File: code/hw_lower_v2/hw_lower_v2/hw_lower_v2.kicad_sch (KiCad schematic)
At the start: 26 parts, among them J1 Screw_Terminal_01x01, J2 Screw_Terminal_01x01, J3 Screw_Terminal_01x01, J4 Screw_Terminal_01x01, J5 Screw_Terminal_01x01, J6 Screw_Terminal_01x01, J7 Conn_01x06_Pin, J8 Conn_02x20_Odd_Even

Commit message: have one project part library
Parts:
- J1, J2, J3, J4, J5, J6: footprint JLCPCB:CONN-TH_T44001 -> multi_new:CONN-TH_T44001
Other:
- moved on the sheet: J1, J2, J3

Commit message: routed most of the board
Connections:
- net AC/GFCI_CALIBRATE: now also J8.9 (Pin_9); no longer J8.21 (Pin_21)
- net AC/GFCI_FAULT: now also J8.11 (Pin_11); no longer J8.19 (Pin_19)
- net AC/GFCI_TEST: now also J8.7 (Pin_7); no longer J8.23 (Pin_23)
- net AC/POWER_MEASUREMENT_INFO: now also J8.19 (Pin_19); no longer J8.11 (Pin_11)

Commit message: layout 99% finished
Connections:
- net +12V: now also J8.21 (Pin_21), J8.23 (Pin_23); no longer J8.1 (Pin_1)
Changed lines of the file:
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@@
 	)
 	(junction
+		(at 240.03 93.98)
+		(diameter 0)
+		(color 0 0 0 0)
+	)
+	(junction
 		(at 257.81 81.28)
 		(diameter 0)
@@
 	(wire
 		(pts
+			(xy 240.03 93.98) (xy 240.03 96.52)
+		)
+		(stroke
+			(width 0)
+			(type default)
+		)
+	)
+	(wire
+		(pts
 			(xy 69.85 49.53) (xy 69.85 68.58)
 		)
@@
 	(wire
 		(pts
+			(xy 240.03 93.98) (xy 242.57 93.98)
+		)
+		(stroke
+			(width 0)
+			(type default)
+		)
+	)
+	(wire
+		(pts
 			(xy 240.03 71.12) (xy 242.57 71.12)
 		)
@@
 	(wire
 		(pts
-			(xy 240.03 68.58) (xy 242.57 68.58)
+			(xy 257.81 96.52) (xy 257.81 99.06)
 		)
 		(stroke
@@
 	(wire
 		(pts
-			(xy 257.81 96.52) (xy 257.81 99.06)
+			(xy 255.27 78.74) (xy 257.81 78.74)
 		)
 		(stroke
@@
 	(wire
 		(pts
-			(xy 255.27 78.74) (xy 257.81 78.74)
+			(xy 242.57 96.52) (xy 240.03 96.52)
 		)
 		(stroke
@@
 	)
 	(symbol
-		(lib_id "power:+12V")
-		(at 240.03 68.58 90)
-		(unit 1)
-		(exclude_from_sim no)
-		(in_bom yes)
-		(on_board yes)
-		(dnp no)
-		(fields_autoplaced yes)
-		(property "Reference" "#PWR03"
-			(at 243.84 68.58 0)
-			(effects
-				(font
-					(size 1.27 1.27)
-				)
-				(hide yes)
-			)
-		)
-		(property "Value" "+12V"
-			(at 236.22 68.5799 90)
-			(effects
-				(font
-					(size 1.27 1.27)
-				)
-				(justify left)
-			)
-		)
-		(property "Footprint" ""
-			(at 240.03 68.58 0)
-			(effects
-				(font
-					(size 1.27 1.27)
-				)
-				(hide yes)
-			)
-		)
-		(property "Datasheet" ""
-			(at 240.03 68.58 0)
-			(effects
-				(font
-					(size 1.27 1.27)
-				)
-				(hide yes)
-			)
-		)
-		(property "Description" "Power symbol creates a global label with name \"+12V\""
-			(at 240.03 68.58 0)
-			(effects
-				(font
-					(size 1.27 1.27)
-				)
-				(hide yes)
-			)
-		)
-		(pin "1"
-		)
-		(instances
-			(project "hw_lower_v2"
-				(path "/c5175f1c-553a-46da-abbd-483c59ad8dfa"
-					(reference "#PWR03")
-					(unit 1)
-				)
-			)
-		)
-	)
-	(symbol
 		(lib_id "Connector:Conn_01x06_Pin")
 		(at 36.83 109.22 0)
@@
 					(unit 1)
 				)
+			)
+		)
+	)
+	(symbol
+		(lib_id "power:+12V")
+		(at 240.03 93.98 90)
+		(unit 1)
+		(exclude_from_sim no)
+		(in_bom yes)
+		(on_board yes)
+		(dnp no)
+		(fields_autoplaced yes)
+		(property "Reference" "#PWR03"
+			(at 243.84 93.98 0)
+			(effects
+				(font
+					(size 1.27 1.27)
+				)
+				(hide yes)
+			)
+		)
+		(property "Value" "+12V"
+			(at 236.22 93.9799 90)
+			(effects
+				(font
+					(size 1.27 1.27)
+				)
+				(justify left)
+			)
+		)
+		(property "Footprint" ""
+			(at 240.03 93.98 0)
+			(effects
+				(font
+					(size 1.27 1.27)
+				)
+				(hide yes)
+			)
+		)
+		(property "Datasheet" ""
+			(at 240.03 93.98 0)
+			(effects
+				(font
+					(size 1.27 1.27)
+				)
+				(hide yes)
+			)
+		)
+		(property "Description" "Power symbol creates a global label with name \"+12V\""
+			(at 240.03 93.98 0)
+			(effects
+				(font
+					(size 1.27 1.27)
+				)
+				(hide yes)
+			)
+		)
+		(pin "1"
+		)
+		(instances
+			(project "hw_lower_v2"
+				(path "/c5175f1c-553a-46da-abbd-483c59ad8dfa"
+					(reference "#PWR03")
+					(unit 1)
+				)

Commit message: simplify component values
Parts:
- R2, R4, R6: value 100K -> 10K; LCSC C25803 -> C25804
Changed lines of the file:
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@@
 			)
 		)
-		(property "Value" "100K"
+		(property "Value" "10K"
 			(at 232.918 148.082 0)
 			(effects
@@
 			)
 		)
-		(property "LCSC" "C25803"
+		(property "LCSC" "C25804"
 			(at 237.49 147.32 0)
 			(effects
@@
 			)
 		)
-		(property "Value" "100K"
+		(property "Value" "10K"
 			(at 251.206 148.336 0)
 			(effects
@@
 			)
 		)
-		(property "LCSC" "C25803"
+		(property "LCSC" "C25804"
 			(at 255.27 147.32 0)
 			(effects
@@
 			)
 		)
-		(property "Value" "100K"
+		(property "Value" "10K"
 			(at 242.316 148.336 0)
 			(effects
@@
 			)
 		)
-		(property "LCSC" "C25803"
+		(property "LCSC" "C25804"
 			(at 246.38 147.32 0)
 			(effects

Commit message: made a full reposition of the whole pcb. When I get everything working, the milkv module can be on the bottom pcb and all the device specific devices can be on the other pcb. Also now conceptualy, the current board can be broken onto two, and be made into a thin long one
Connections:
- net EVSE control and status/CONTROL_PILOT_OUT: now also J7.5 (Pin_5); no longer J7.1 (Pin_1)
- net EVSE control and status/LOCK_SENSE_GND: now also J7.2 (Pin_2); no longer J7.6 (Pin_6)
- net EVSE control and status/LOCK_SENSE_OUT: now also J7.1 (Pin_1); no longer J7.5 (Pin_5)
- net EVSE control and status/PROXIMITY_PILOT: now also J7.6 (Pin_6); no longer J7.2 (Pin_2)
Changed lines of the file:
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@@
 	(wire
 		(pts
+			(xy 41.91 104.14) (xy 72.39 104.14)
+		)
+		(stroke
+			(width 0)
+			(type default)
+		)
+	)
+	(wire
+		(pts
 			(xy 209.55 78.74) (xy 209.55 86.36)
 		)
@@
 	(wire
 		(pts
-			(xy 41.91 77.47) (xy 44.45 77.47)
+			(xy 41.91 106.68) (xy 72.39 106.68)
 		)
 		(stroke
@@
 	(wire
 		(pts
-			(xy 72.39 111.76) (xy 66.04 111.76)
+			(xy 41.91 114.3) (xy 72.39 114.3)
 		)
 		(stroke
@@
 	(wire
 		(pts
-			(xy 255.27 76.2) (xy 257.81 76.2)
+			(xy 41.91 77.47) (xy 44.45 77.47)
 		)
 		(stroke
@@
 	(wire
 		(pts
-			(xy 119.38 81.28) (xy 207.01 81.28)
+			(xy 255.27 76.2) (xy 257.81 76.2)
 		)
 		(stroke
@@
 	(wire
 		(pts
-			(xy 119.38 71.12) (xy 214.63 71.12)
+			(xy 119.38 81.28) (xy 207.01 81.28)
 		)
 		(stroke
@@
 	(wire
 		(pts
-			(xy 257.81 101.6) (xy 257.81 104.14)
+			(xy 119.38 71.12) (xy 214.63 71.12)
 		)
 		(stroke
@@
 	(wire
 		(pts
-			(xy 261.62 114.3) (xy 261.62 124.46)
+			(xy 257.81 101.6) (xy 257.81 104.14)
 		)
 		(stroke
@@
 	(wire
 		(pts
-			(xy 66.04 111.76) (xy 66.04 106.68)
+			(xy 261.62 114.3) (xy 261.62 124.46)
 		)
 		(stroke
@@
 	(wire
 		(pts
-			(xy 60.96 111.76) (xy 41.91 111.76)
-		)
-		(stroke
-			(width 0)
-			(type default)
-		)
-	)
-	(wire
-		(pts
 			(xy 186.69 101.6) (xy 242.57 101.6)
 		)
@@
 	(wire
 		(pts
-			(xy 72.39 125.73) (xy 55.88 125.73)
+			(xy 240.03 121.92) (xy 240.03 142.24)
 		)
 		(stroke
@@
 	(wire
 		(pts
-			(xy 240.03 121.92) (xy 240.03 142.24)
+			(xy 41.91 85.09) (xy 44.45 85.09)
 		)
 		(stroke
@@
 	(wire
 		(pts
-			(xy 41.91 85.09) (xy 44.45 85.09)
+			(xy 41.91 116.84) (xy 72.39 116.84)
 		)
 		(stroke
@@
 	(wire
 		(pts
-			(xy 55.88 125.73) (xy 55.88 116.84)
-		)
-		(stroke
-			(width 0)
-			(type default)
-		)
-	)
-	(wire
-		(pts
 			(xy 255.27 73.66) (xy 257.81 73.66)
 		)
@@
 	(wire
 		(pts
-			(xy 60.96 120.65) (xy 60.96 111.76)
+			(xy 41.91 72.39) (xy 72.39 72.39)
 		)
 		(stroke
@@
 	(wire
 		(pts
-			(xy 41.91 72.39) (xy 72.39 72.39)
+			(xy 41.91 111.76) (xy 72.39 111.76)
 		)
 		(stroke
@@
 	(wire
 		(pts
-			(xy 55.88 116.84) (xy 41.91 116.84)
-		)
-		(stroke
-			(width 0)
-			(type default)
-		)
-	)
-	(wire
-		(pts
 			(xy 219.71 76.2) (xy 219.71 66.04)
 		)
@@
 	(wire
 		(pts
-			(xy 66.04 106.68) (xy 41.91 106.68)
+			(xy 191.77 114.3) (xy 242.57 114.3)
 		)
 		(stroke
@@
 	(wire
 		(pts
-			(xy 191.77 114.3) (xy 242.57 114.3)
+			(xy 259.08 121.92) (xy 259.08 116.84)
 		)
 		(stroke
@@
 	(wire
 		(pts
-			(xy 259.08 121.92) (xy 259.08 116.84)
+			(xy 41.91 87.63) (xy 72.39 87.63)
 		)
 		(stroke
@@
 	(wire
 		(pts
-			(xy 41.91 87.63) (xy 72.39 87.63)
+			(xy 41.91 109.22) (xy 72.39 109.22)
 		)
 		(stroke
@@
 	(wire
 		(pts
-			(xy 63.5 109.22) (xy 41.91 109.22)
-		)
-		(stroke
-			(width 0)
-			(type default)
-		)
-	)
-	(wire
-		(pts
 			(xy 119.38 111.76) (xy 186.69 111.76)
 		)
@@
 	(wire
 		(pts
-			(xy 63.5 118.11) (xy 63.5 109.22)
-		)
-		(stroke
-			(width 0)
-			(type default)
-		)
-	)
-	(wire
-		(pts
 			(xy 262.89 71.12) (xy 262.89 68.58)
 		)
@@
 	(wire
 		(pts
-			(xy 72.39 118.11) (xy 63.5 118.11)
-		)
-		(stroke
-			(width 0)
-			(type default)
-		)
-	)
-	(wire
-		(pts
 			(xy 194.31 116.84) (xy 242.57 116.84)
 		)
@@
 	(wire
 		(pts
-			(xy 72.39 120.65) (xy 60.96 120.65)
-		)
-		(stroke
-			(width 0)
-			(type default)
-		)
-	)
-	(wire
-		(pts
 			(xy 214.63 81.28) (xy 242.57 81.28)
 		)
@@
 	(wire
 		(pts
-			(xy 72.39 123.19) (xy 58.42 123.19)
-		)
-		(stroke
-			(width 0)
-			(type default)
-		)
-	)
-	(wire
-		(pts
 			(xy 246.38 142.24) (xy 246.38 143.51)
 		)
@@
 	(wire
 		(pts
-			(xy 58.42 114.3) (xy 41.91 114.3)
-		)
-		(stroke
-			(width 0)
-			(type default)
-		)
-	)
-	(wire
-		(pts
-			(xy 58.42 123.19) (xy 58.42 114.3)
-		)
-		(stroke
-			(width 0)
-			(type default)
-		)
-	)
-	(wire
-		(pts
 			(xy 257.81 78.74) (xy 257.81 81.28)
 		)
@@
 		)
 	)
-	(wire
-		(pts
-			(xy 41.91 104.14) (xy 72.39 104.14)
-		)
-		(stroke
-			(width 0)
-			(type default)
-		)
-	)
 	(text "BOARD VERSION: V0"
 		(exclude_from_sim no)
@@
 		)
 		(pin "PROXIMITY_PILOT" input
-			(at 72.39 111.76 180)
+			(at 72.39 116.84 180)
 			(effects
 				(font
@@
 		)
 		(pin "LOCK_A_OUT" input
-			(at 72.39 118.11 180)
+			(at 72.39 109.22 180)
 			(effects
 				(font
@@
 		)
 		(pin "LOCK_B_OUT" input
-			(at 72.39 120.65 180)
+			(at 72.39 111.76 180)
 			(effects
 				(font
@@
 		)
 		(pin "CONTROL_PILOT_OUT" input
-			(at 72.39 104.14 180)
+			(at 72.39 114.3 180)
 			(effects
 				(font
@@
 		)
 		(pin "LOCK_SENSE_GND" input
-			(at 72.39 125.73 180)
+			(at 72.39 106.68 180)
 			(effects
 				(font
@@
 		)
 		(pin "LOCK_SENSE_OUT" input
-			(at 72.39 123.19 180)
+			(at 72.39 104.14 180)
 			(effects
 				(font

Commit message: Relalaid out the LV part of the board.
One or two small things left to do.
Prepared for the 2.0 version of the PCB where the duo01 module can be
put on the lower board.
Also it is possible to make a sandwitch situation, and make a long thin
product.
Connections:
- net +5V: no longer names the net of J8.3 (Pin_3)
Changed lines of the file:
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@@
-	(wire
-		(pts
-			(xy 240.03 71.12) (xy 242.57 71.12)
-		)
-		(stroke
-			(width 0)
-			(type default)
-		)
-	)
 	(wire
 		(pts
@@
 					(unit 1)
 				)
-			)
-		)
-	)
-	(symbol
-		(lib_id "power:+5V")
-		(at 240.03 71.12 90)
-		(unit 1)
-		(exclude_from_sim no)
-		(in_bom yes)
-		(on_board yes)
-		(dnp no)
-		(property "Reference" "#PWR04"
-			(at 243.84 71.12 0)
-			(effects
-				(font
-					(size 1.27 1.27)
-				)
-				(hide yes)
-			)
-		)
-		(property "Value" "+5V"
-			(at 232.918 71.12 90)
-			(effects
-				(font
-					(size 1.27 1.27)
-				)
-			)
-		)
-		(property "Footprint" ""
-			(at 240.03 71.12 0)
-			(effects
-				(font
-					(size 1.27 1.27)
-				)
-				(hide yes)
-			)
-		)
-		(property "Datasheet" ""
-			(at 240.03 71.12 0)
-			(effects
-				(font
-					(size 1.27 1.27)
-				)
-				(hide yes)
-			)
-		)
-		(property "Description" "Power symbol creates a global label with name \"+5V\""
-			(at 240.03 71.12 0)
-			(effects
-				(font
-					(size 1.27 1.27)
-				)
-				(hide yes)
-			)
-		)
-		(pin "1"
-		)
-		(instances
-			(project "hw_lower_v2"
-				(path "/c5175f1c-553a-46da-abbd-483c59ad8dfa"
-					(reference "#PWR04")
-					(unit 1)
-				)

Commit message: almost ready :-)
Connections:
- net +3.3V: now also J8.1 (Pin_1), J8.3 (Pin_3)
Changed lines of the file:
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@@
+	)
+	(junction
+		(at 240.03 71.12)
+		(diameter 0)
+		(color 0 0 0 0)
 	)
 	(junction
@@
 		(color 0 0 0 0)
 	)
+	(junction
+		(at 240.03 73.66)
+		(diameter 0)
+		(color 0 0 0 0)
+	)
+	(wire
+		(pts
+			(xy 240.03 68.58) (xy 240.03 71.12)
+		)
+		(stroke
+			(width 0)
+			(type default)
+		)
+	)
 	(wire
 		(pts
@@
 	(wire
 		(pts
+			(xy 240.03 71.12) (xy 240.03 73.66)
+		)
+		(stroke
+			(width 0)
+			(type default)
+		)
+	)
+	(wire
+		(pts
 			(xy 257.81 99.06) (xy 257.81 101.6)
 		)
@@
 	(wire
 		(pts
+			(xy 240.03 71.12) (xy 242.57 71.12)
+		)
+		(stroke
+			(width 0)
+			(type default)
+		)
+	)
+	(wire
+		(pts
 			(xy 257.81 91.44) (xy 257.81 93.98)
 		)
@@
 		)
 		(stroke
+			(width 0)
+			(type default)
+		)
+	)
+	(wire
+		(pts
+			(xy 242.57 68.58) (xy 240.03 68.58)
+		)
+		(stroke

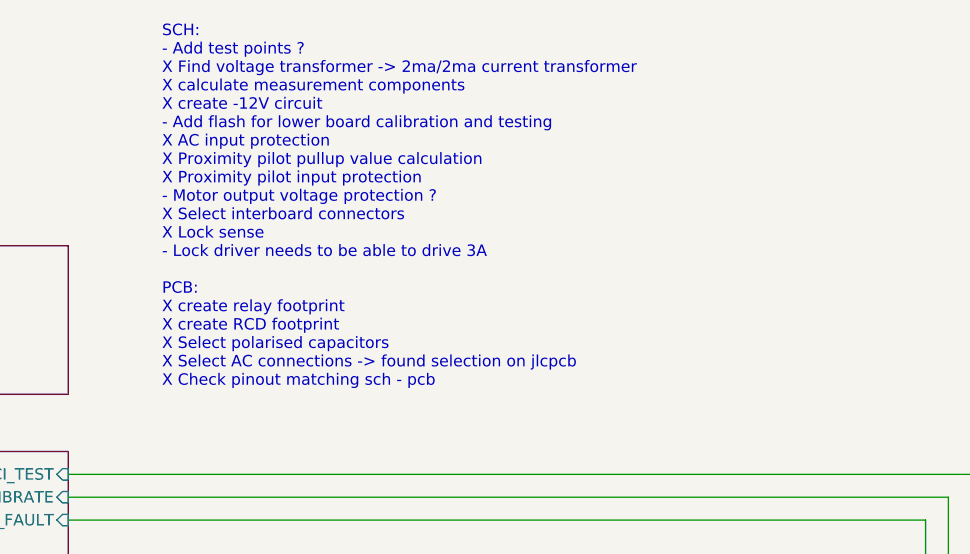
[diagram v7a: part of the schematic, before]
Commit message: add JLCPCB tooling holes and simplify further
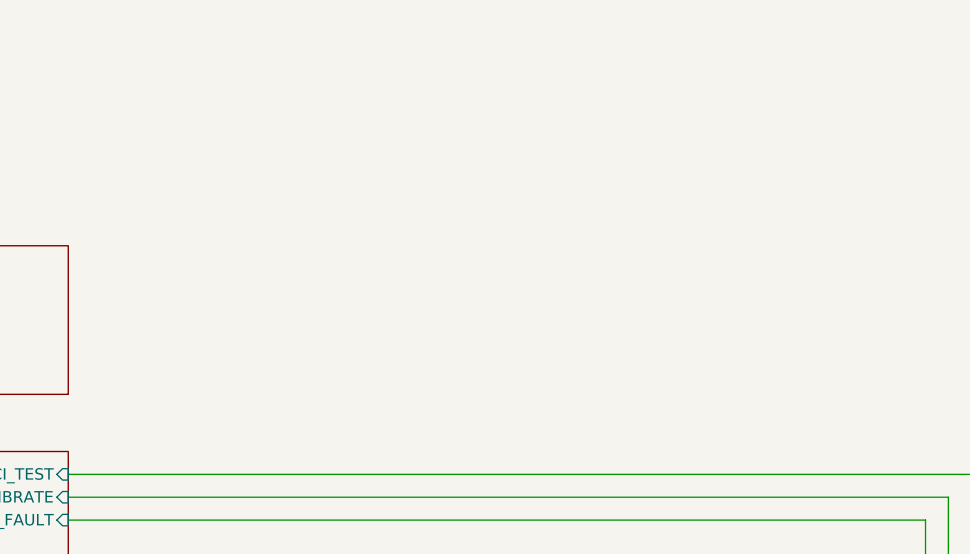
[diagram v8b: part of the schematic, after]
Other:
- note removed: "SCH: - Add test points ? X Find voltage transformer -> 2ma/2ma current transformer X calculate measurement components X create -12V circuit - Add flash for lower board calibration and testing X AC input protection X Proximity pilot pullup value calculation X Proximity pilot input protection - Motor output voltage protection ? X Select interboard connectors X Lock sense - Lock driver needs to be a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"
- title: EVSE -> BlueEVSE
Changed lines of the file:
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@@
 	(paper "A4")
 	(title_block
-		(title "EVSE")
+		(title "BlueEVSE")
 		(date "2024-07-14")
 		(rev "V2")
@@
 		)
 	)
-	(text "SCH:\n- Add test points ?\nX Find voltage transformer -> 2ma/2ma current transformer\nX calculate measurement components\nX create -12V circuit\n- Add flash for lower board calibration and testing\nX AC input protection\nX Proximity pilot pullup value calculation\nX Proximity pilot input protection\n- Motor output voltage protection ?\nX Select interboard connectors\nX Lock sense\n- Lock driver needs to be able to drive 3A\n\nPCB: \nX create relay footprint\nX create RCD footprint\nX Select polarised capacitors\nX Select AC connections -> found selection on jlcpcb\nX Check pinout matching sch - pcb\n"
-		(exclude_from_sim no)
-		(at 129.794 36.322 0)
-		(effects
-			(font
-				(size 1.27 1.27)
-			)
-			(justify left)
-		)
-	)
